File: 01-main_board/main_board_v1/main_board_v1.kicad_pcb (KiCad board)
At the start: 4 copper layers, 96.4 x 65.3 mm, 152 parts, among them IC1 MAX6105EUR+T, IC10 ESP32-S3, IC11 TPS62173DSGT, IC2 LP5907MFX-2.5_NOPB, IC4 SPX3819S-L_TR, IC5 INA827AIDGK, IC6 AD7175-8BCPZ-RL7, IC7 INA827AIDGK, IC8 AD8591ARTZ-REEL7, IC9 LSF0108PWR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

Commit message: Almost done, just grounding layout
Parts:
- moved C47 5.52 mm to (53.2, 69.5)
- moved C48 5.52 mm to (55.2, 67.8)
- moved C49 5.52 mm to (56.5, 83.5)
- moved C5 5.52 mm to (51.4, 72.1)
- moved C50 5.52 mm to (58.5, 83.5)
- moved C6 5.52 mm to (46.7, 74.5)
- moved IC10 5.52 mm to (57.5, 75.5)
- moved L2 5.52 mm to (49.2, 73.5)
- moved R100 5.52 mm to (52.0, 75.0)
- moved R101 5.52 mm to (58.0, 70.1)
- moved TP8 5.52 mm to (59.0, 68.5)
- moved Y1 5.52 mm to (55.5, 69.8)
- moved Y2 5.52 mm to (57.5, 81.5)
- moved NT3 5.52 mm to (50.9, 68.0)
- moved C25 0.40 mm to (43.0, 74.9)
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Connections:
- C5 pad 2: GNDA -> GNDD
- C6 pad 2: GNDA -> GNDD
- L3 pad 1: GNDA -> GNDD
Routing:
- net GNDD: track 42.9 -> 56.5 mm, vias 25 -> 57
- net PGND: track 35.7 -> 42.9 mm, vias 18 -> 20
- net Net-(C25-Pad2): track 0.00 -> 5.79 mm
- net MISO_ESP: track 40.9 -> 46.4 mm
- net SCLK_ESP: track 42.5 -> 48.0 mm
- net CS_ESP: track 22.5 -> 28.0 mm
- net MOSI_ESP: track 44.5 -> 49.1 mm
- net Net-(IC10-LNA_IN): track 0.00 -> 4.24 mm
- net GNDA: track 51.4 -> 55.6 mm, vias 27 -> 30
- net Net-(C25-Pad1): track 0.00 -> 2.52 mm
- net Net-(AE1-FEED): track 0.00 -> 2.45 mm
- net 3V3: track 88.4 -> 86.2 mm, vias 6 -> 7
- added copper zone on F.Cu, net GNDD

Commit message: Updated PCB from schematic for antenna with NC end
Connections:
- AE1 pad 2: GNDA -> unconnected-(AE1-PCB_Trace-Pad2)
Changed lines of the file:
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@@
 	(net 199 "GNDD")
 	(net 200 "B-")
+	(net 201 "unconnected-(AE1-PCB_Trace-Pad2)")
 	(footprint "Package_TO_SOT_SMD:SOT-23-3"
 		(layer "F.Cu")
@@
 			(size 0.8 1.6)
 			(layers "F.Cu" "F.Mask" "F.Paste")
-			(net 1 "GNDA")
+			(net 201 "unconnected-(AE1-PCB_Trace-Pad2)")
 			(pinfunction "PCB_Trace")
-			(pintype "passive")
+			(pintype "passive+no_connect")
 			(solder_mask_margin 0.102)
 		)

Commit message: Changes
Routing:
- net usb-: track 50.5 -> 46.8 mm
- net usb+: track 49.1 -> 46.2 mm
- net GNDD: vias 57 -> 93

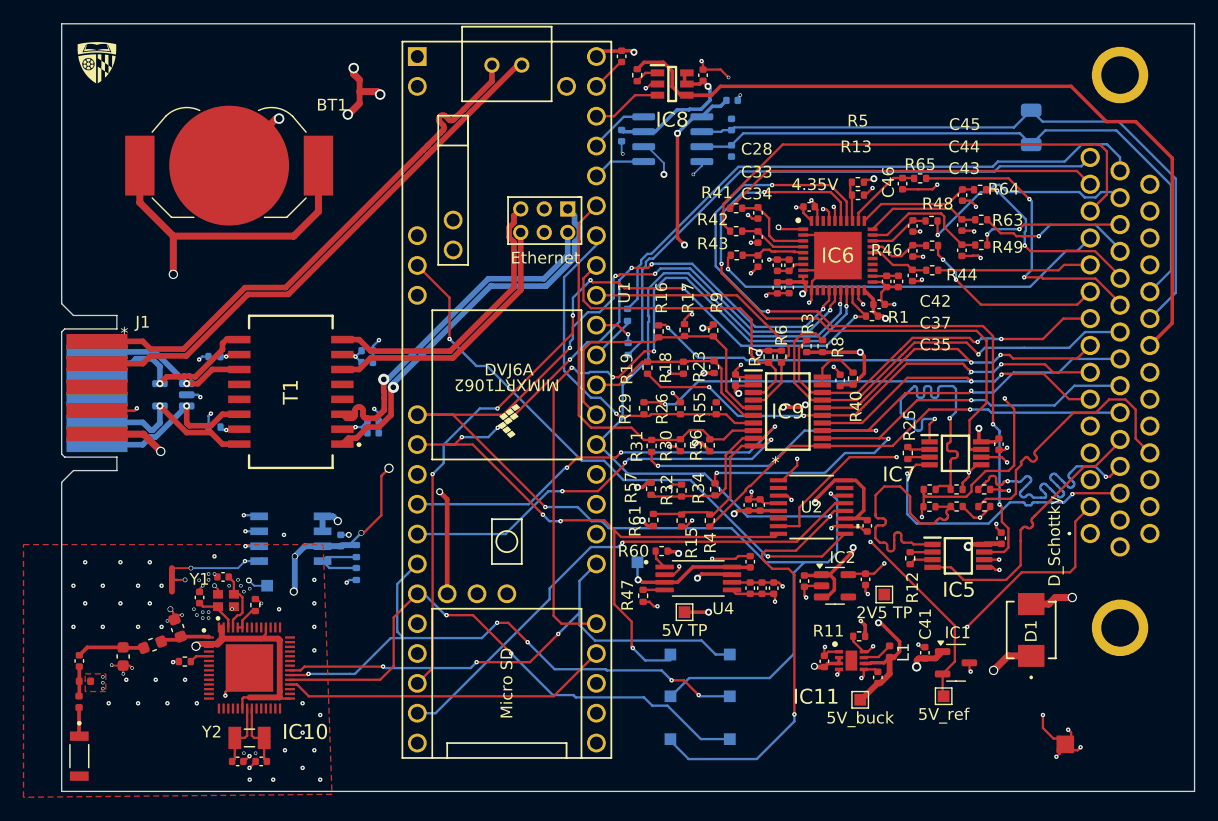
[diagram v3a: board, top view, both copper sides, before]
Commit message: added decoupling caps for esp32s3 and resolved drc errors
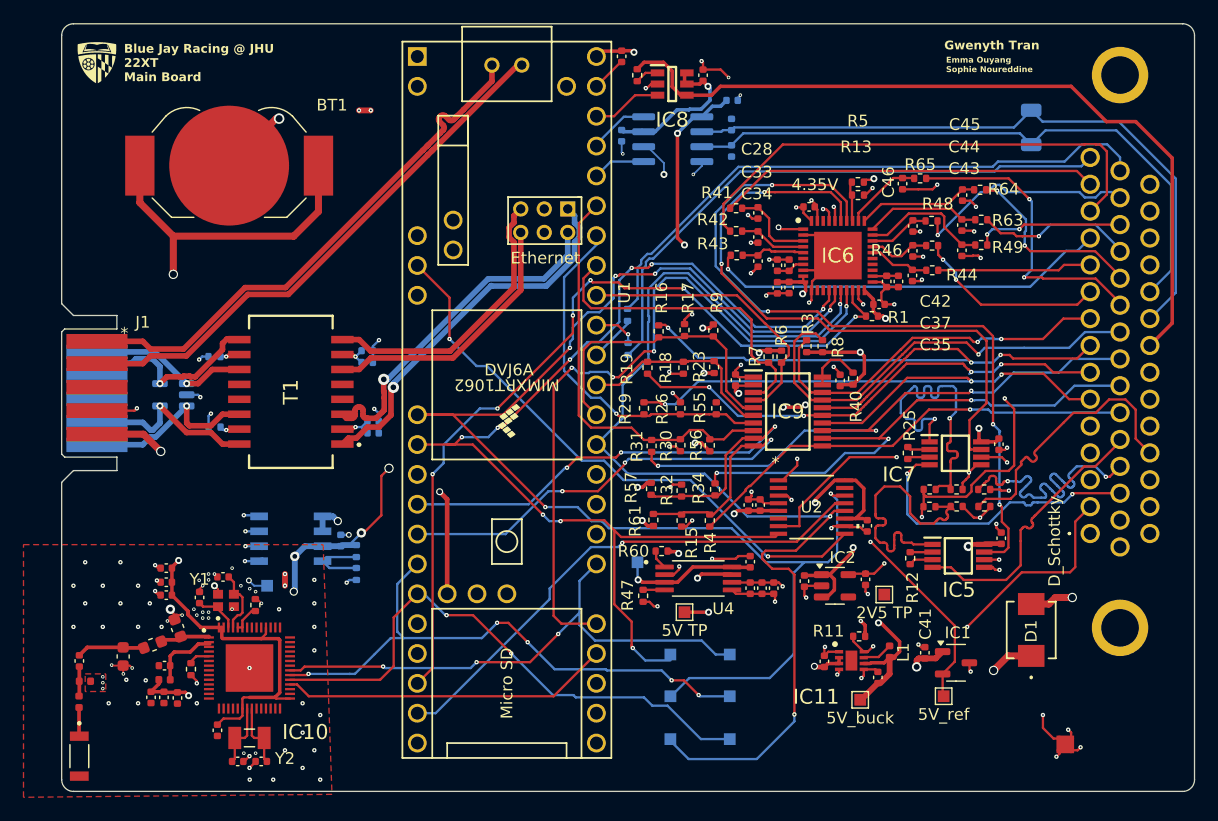
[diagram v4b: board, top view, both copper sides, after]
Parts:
- added C53: 2.2uF, Capacitor_SMD:C_0402_1005Metric, F.Cu at (51.4, 78.0)
- added C54: 2.2uF, Capacitor_SMD:C_0402_1005Metric, F.Cu at (50.2, 78.0)
- added C55: 0.1uF, Capacitor_SMD:C_0402_1005Metric, F.Cu at (49.1, 78.0)
- added C56: 0.1uF, Capacitor_SMD:C_0402_1005Metric, F.Cu at (50.2, 75.3)
- added C57: 2.2uF, Capacitor_SMD:C_0402_1005Metric, F.Cu at (50.4, 69.3)
- added C58: 0.1uF, Capacitor_SMD:C_0402_1005Metric, F.Cu at (50.4, 68.2)
- added C59: 10nF, Capacitor_SMD:C_0402_1005Metric, F.Cu at (50.4, 67.0)
- added C60: 0.1uF, Capacitor_SMD:C_0402_1005Metric, F.Cu at (54.8, 80.8)
- added L5: 2nH, Inductor_SMD:L_0402_1005Metric, F.Cu at (50.2, 76.5)
- NT2, NT3: footprint NetTie:NetTie-3_SMD_Pad0.5mm -> NetTie:NetTie-2_SMD_Pad0.5mm
- moved NT3 9.62 mm to (60.5, 68.0), turned to -90 degrees
- moved NT2 1.66 mm to (67.3, 28.1), turned to 0 degrees
- moved R100 0.83 mm to (52.5, 75.6), turned to 90 degrees
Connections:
- BT1 pad 2: PGND -> GNDA
- IC10 pad 2: 3V3 -> Net-(IC10-VDD3P3_1)
- IC10 pad 3: 3V3 -> Net-(IC10-VDD3P3_1)
- NT3 pad 1: GNDA -> PGND
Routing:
- net PGND: track 42.9 -> 28.7 mm, vias 20 -> 17
- net 3V3: track 86.2 -> 100.2 mm, vias 7 -> 8
- net Net-(IC10-VDD3P3_1): track 0.00 -> 5.81 mm
- net GNDA: track 55.6 -> 60.5 mm, vias 30 -> 31
- net GNDD: track 56.5 -> 51.7 mm, vias 93 -> 90
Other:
- outline, holes or cut-outs redrawn
- board text added: "Blue Jay Racing @ JHU 22XT Main Board"
- board text added: "Emma Ouyang Sophie Noureddine"
- board text added: "Gwenyth Tran"

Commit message: finalized bom, cli, gerber files
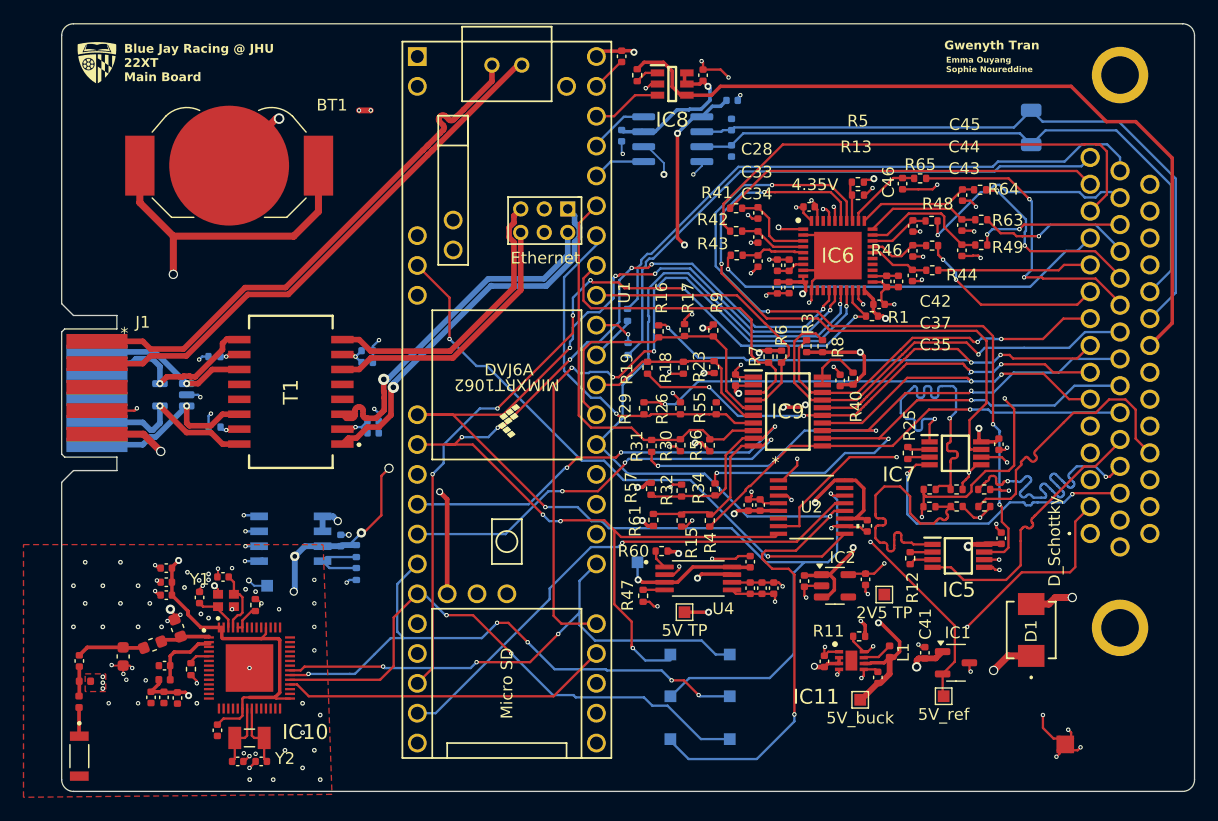
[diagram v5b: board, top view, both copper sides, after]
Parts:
- removed NT3: NetTie_3_Tee, NetTie:NetTie-2_SMD_Pad0.5mm
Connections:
- C7 pad 1: PGND -> GNDD
- IC4 pad 5: PGND -> GNDD
- IC4 pad 6: PGND -> GNDD
- IC4 pad 7: PGND -> GNDD
- IC4 pad 8: PGND -> GNDD
- R45 pad 2: PGND -> GNDD
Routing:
- net GNDD: track 51.7 -> 60.2 mm, vias 90 -> 92
- net PGND: track 28.7 -> 20.5 mm, vias 17 -> 10

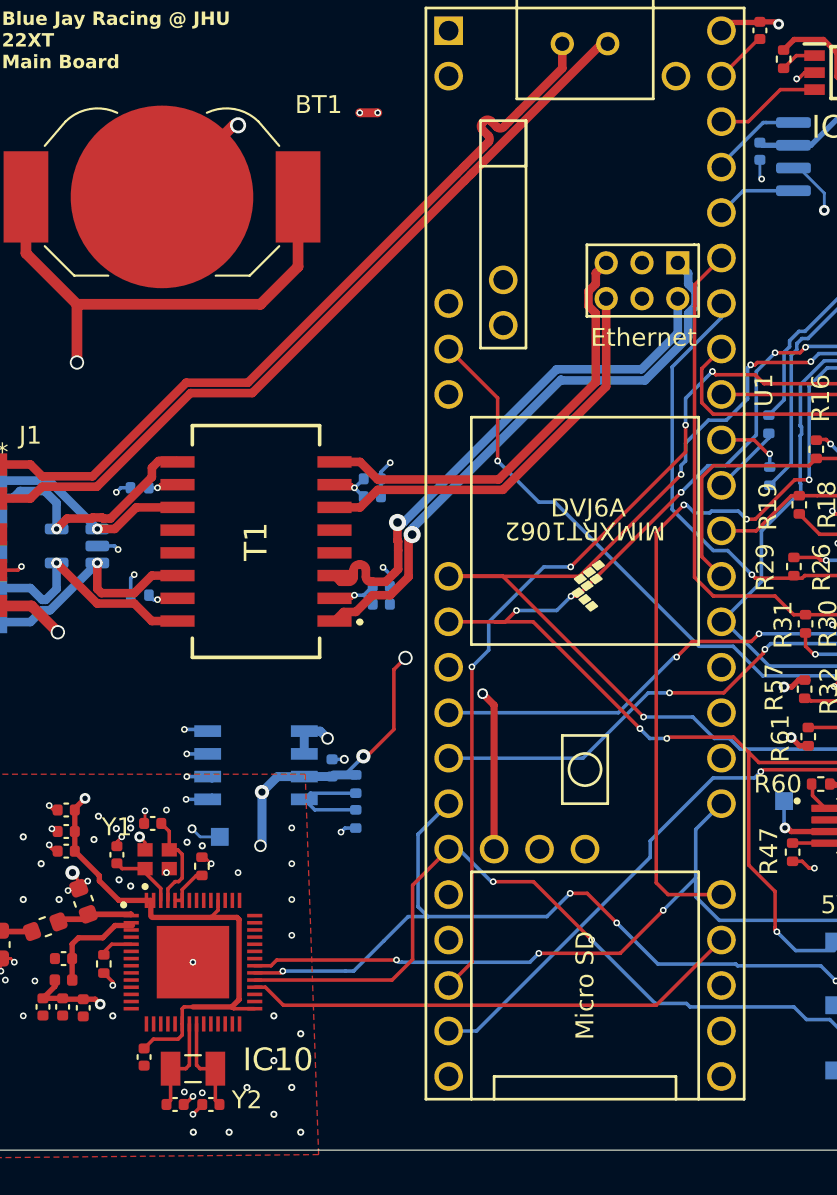
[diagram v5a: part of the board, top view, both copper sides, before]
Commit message: Began changing vias
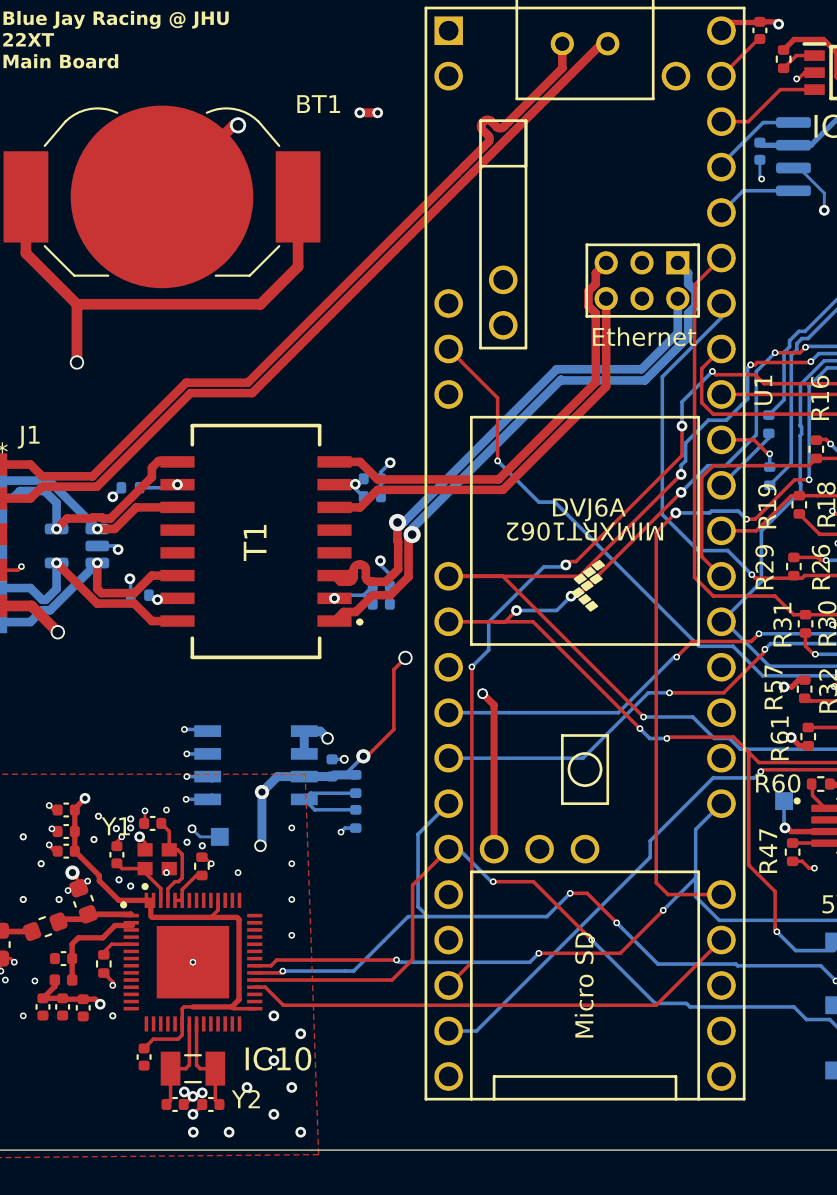
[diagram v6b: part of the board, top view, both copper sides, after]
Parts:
- moved R28 0.51 mm to (54.0, 49.0)
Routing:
- net D3_shift: track 30.7 -> 31.7 mm
- net Net-(T1-TXCT): track 1.68 -> 2.19 mm

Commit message: Created mofied bom & cpl
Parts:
- 5v_usb: renamed from TP12; moved to F.Cu
- TP7: value 5V TP -> 5V
- TP8: value 3V3 TP -> 3V3
- TP9: value 2V5 TP -> 2V5
- moved 5v_usb 41.6 mm to (49.5, 59.5), turned to 0 degrees
- moved TP3 31.3 mm to (69.5, 69.5)
- moved TP2 31.0 mm to (69.5, 66.5)
- moved TP5 30.8 mm to (74.1, 53.9)
- moved TP4 29.2 mm to (69.5, 57.5)
- moved TP6 27.3 mm to (85.0, 55.5)
- moved TP1 11.5 mm to (89.5, 67.0)
- moved R31 0.84 mm to (91.7, 55.8)
- moved R56 0.74 mm to (96.7, 55.8)
- moved R30 0.73 mm to (94.2, 55.8)
- moved TP8 0.64 mm to (59.6, 68.3)
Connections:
- C51 pad 2: GNDD -> GNDA
- C52 pad 2: GNDD -> GNDA
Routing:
- net SCLK1: track 97.1 -> 63.5 mm, vias 3 -> 2
- net SCLK_ESP: track 48.0 -> 18.7 mm, vias 2 -> 0
- net MOSI_ESP: track 49.1 -> 20.6 mm, vias 5 -> 0
- net MOSI1: track 115.0 -> 96.6 mm
- net MISO_ESP: track 46.4 -> 34.5 mm
- net MISO1: track 93.5 -> 82.7 mm, vias 9 -> 8
- net GNDA: track 60.5 -> 56.8 mm, vias 31 -> 34
- net 2V5: track 64.9 -> 67.1 mm
- net 5V_usb: track 63.0 -> 64.6 mm
- net GNDD: track 60.1 -> 58.6 mm
- net D4_shift: track 35.3 -> 33.8 mm
- net DN4: track 50.0 -> 50.9 mm
- net AN6: track 19.8 -> 19.3 mm
- net 3V3_teensy: track 71.5 -> 72.0 mm, vias 14 -> 15

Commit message: Re-generated final gerbers
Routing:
- net GNDD: vias 92 -> 134
